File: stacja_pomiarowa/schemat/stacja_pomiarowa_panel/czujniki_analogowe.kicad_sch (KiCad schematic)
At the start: 32 parts, among them J20 Conn_01x03, J21 Conn_01x03, J22 Conn_01x03, J23 Conn_01x03, J24 Conn_01x03, J25 Conn_01x03, J26 Conn_01x03, J27 Conn_01x03, J28 Conn_01x03, J29 Conn_01x03, J30 Conn_01x03, J31 Conn_01x03, J32 Conn_01x03, J33 Conn_01x03, J34 Conn_01x03, J35 Conn_01x03, J36 Conn_01x03, J37 Conn_01x03, J38 Conn_01x03, J39 Conn_01x03, J40 Conn_01x03, J41 Conn_01x03, J42 Conn_01x03, J43 Conn_01x03, J44 Conn_01x03, J45 Conn_01x03, J46 Conn_01x03, J47 Conn_01x03, J48 Conn_01x03, J49 Conn_01x03, J50 Conn_01x03, J51 Conn_01x03

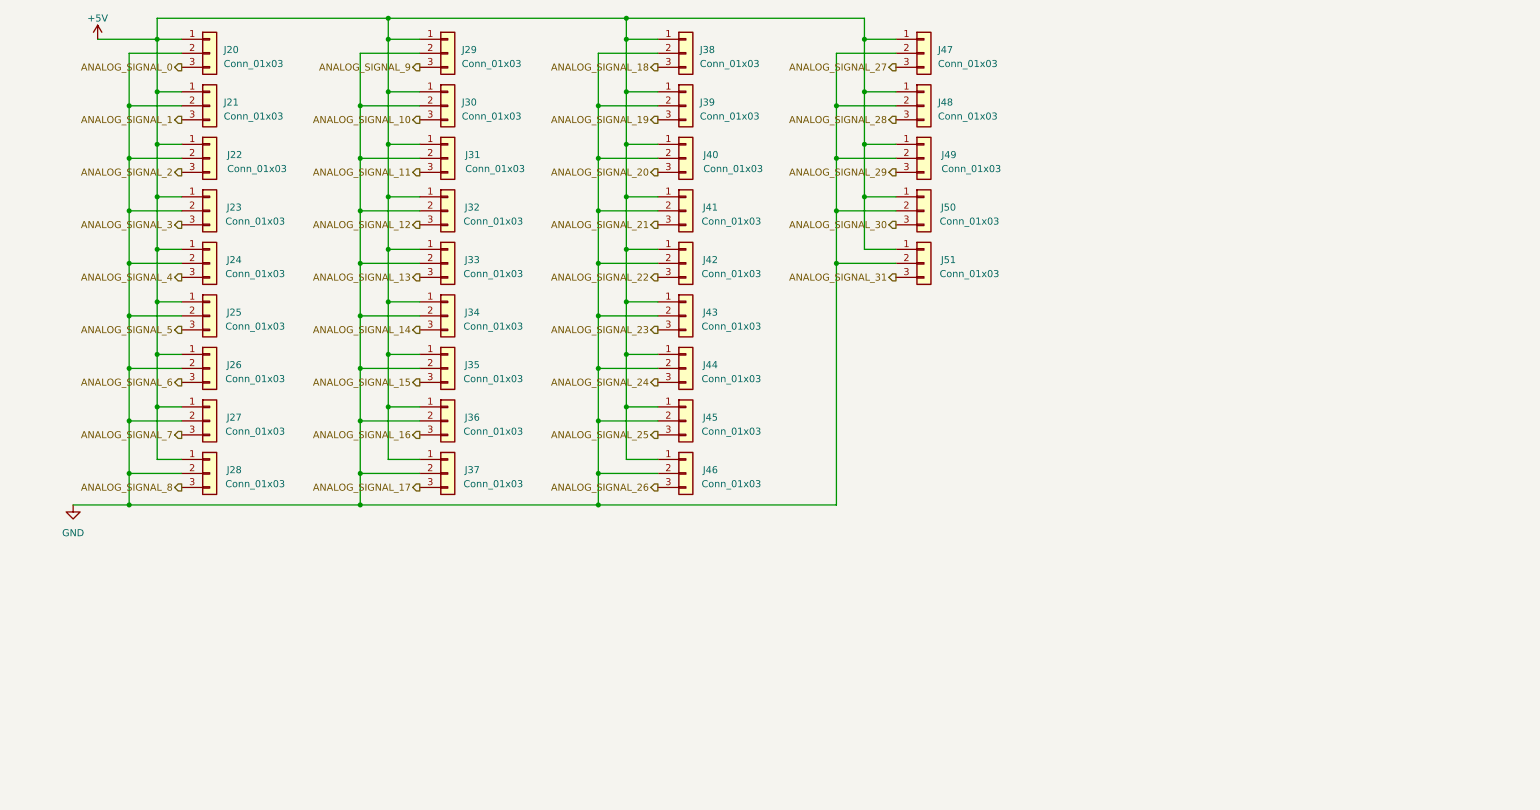
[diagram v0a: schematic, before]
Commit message: Poprawa schematu
Poprzednia numeracja wyjsc analogowych, dodany brakujacy tranzystor Q1, dodane brakujace oporniki podciagajace dla 1-wire i dht11, usuniete oporniki sciagajace dla wyjsc a[0..1] adc - w ten sposob przy niepodlaczonym czujniki nie bedzie stanu niskiego zamiast tego dodane oproniki sciagajace do zlacz dla czujnikow analogowych
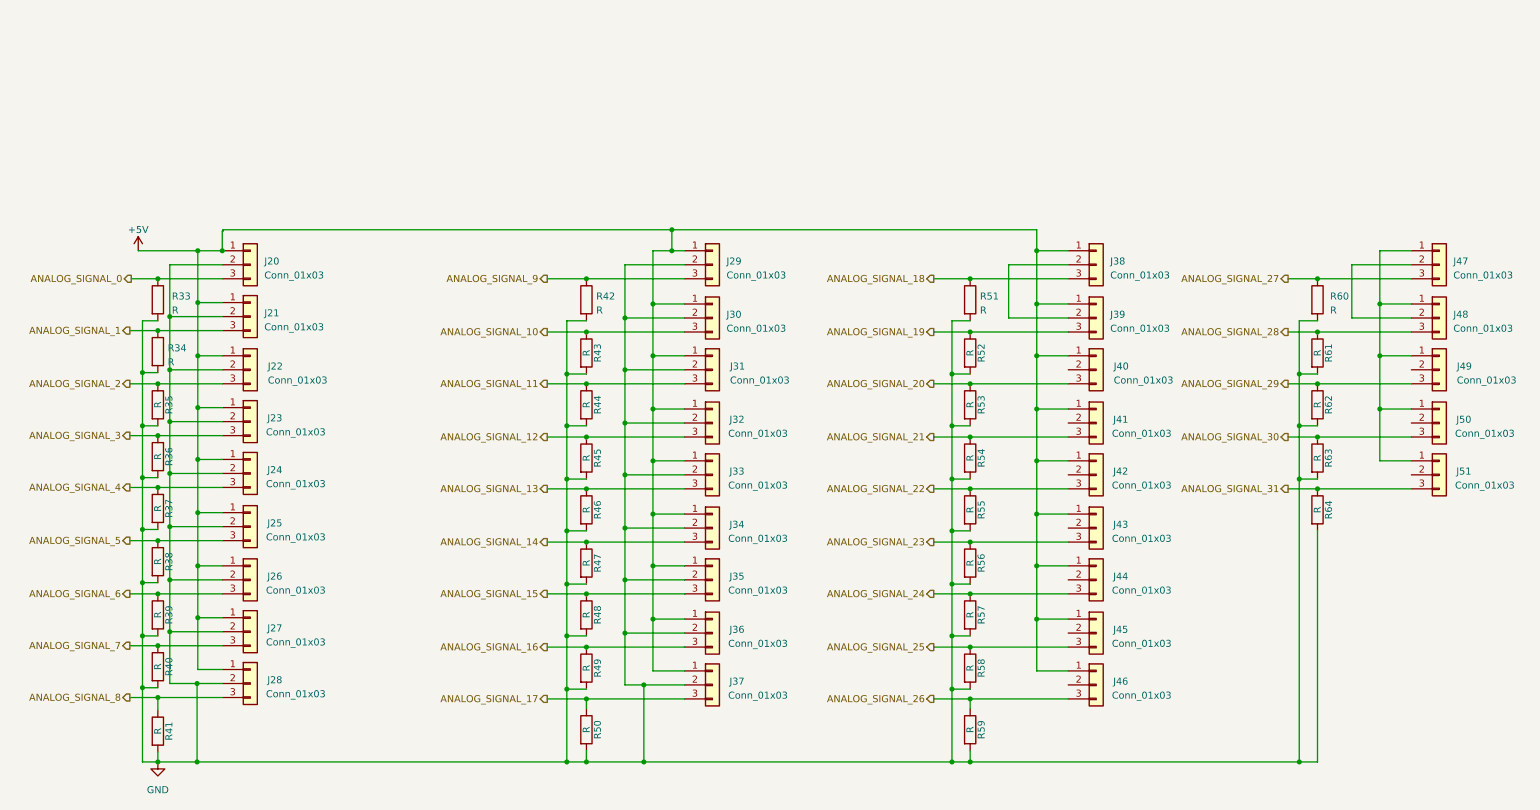
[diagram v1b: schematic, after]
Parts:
- added R33, R34, R35, R36, R37, R38, R39, R40, R41, R42, R43, R44, R45, R46, R47, R48, R49, R50, R51, R52, R53, R54, R55, R56, R57, R58, R59, R60, R61, R62, R63, R64: R, symbol Device:R
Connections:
- net +5V: no longer J47.1 (Pin_1), J48.1 (Pin_1), J49.1 (Pin_1), J50.1 (Pin_1), J51.1 (Pin_1)
- net ANALOG_SIGNAL_0: now also R33.1
- net ANALOG_SIGNAL_1: now also R34.1
- net ANALOG_SIGNAL_10: now also R43.1
- net ANALOG_SIGNAL_11: now also R44.1
- net ANALOG_SIGNAL_12: now also R45.1
- net ANALOG_SIGNAL_13: now also R46.1
- net ANALOG_SIGNAL_14: now also R47.1
- net ANALOG_SIGNAL_15: now also R48.1
- net ANALOG_SIGNAL_16: now also R49.1
- net ANALOG_SIGNAL_17: now also R50.1
- net ANALOG_SIGNAL_18: now also R51.1
- net ANALOG_SIGNAL_19: now also R52.1
- net ANALOG_SIGNAL_2: now also R35.1
- net ANALOG_SIGNAL_20: now also R53.1
- net ANALOG_SIGNAL_21: now also R54.1
- net ANALOG_SIGNAL_22: now also R55.1
- net ANALOG_SIGNAL_23: now also R56.1
- net ANALOG_SIGNAL_24: now also R57.1
- net ANALOG_SIGNAL_25: now also R58.1
- net ANALOG_SIGNAL_26: now also R59.1
- net ANALOG_SIGNAL_27: now also R60.1
- net ANALOG_SIGNAL_28: now also R61.1
- net ANALOG_SIGNAL_29: now also R62.1
- net ANALOG_SIGNAL_3: now also R36.1
- net ANALOG_SIGNAL_30: now also R63.1
- net ANALOG_SIGNAL_31: now also R64.1
- net ANALOG_SIGNAL_4: now also R37.1
- net ANALOG_SIGNAL_5: now also R38.1
- net ANALOG_SIGNAL_6: now also R39.1
- net ANALOG_SIGNAL_7: now also R40.1
- net ANALOG_SIGNAL_8: now also R41.1
- net ANALOG_SIGNAL_9: now also R42.1
- net GND: now also R33.2, R34.2, R35.2, R36.2, R37.2, R38.2, R39.2, R40.2, R41.2, R42.2, R43.2, R44.2, R45.2, R46.2, R47.2, R48.2, R49.2, R50.2, R51.2, R52.2, R53.2, R54.2, R55.2, R56.2, R57.2, R58.2, R59.2, R60.2, R61.2, R62.2, R63.2, R64.2; no longer J38.2 (Pin_2), J39.2 (Pin_2), J40.2 (Pin_2), J41.2 (Pin_2), J42.2 (Pin_2), J43.2 (Pin_2), J44.2 (Pin_2), J45.2 (Pin_2), J46.2 (Pin_2), J47.2 (Pin_2), J48.2 (Pin_2), J49.2 (Pin_2), J50.2 (Pin_2), J51.2 (Pin_2)
- new net: J47.1 (Pin_1), J48.1 (Pin_1), J49.1 (Pin_1), J50.1 (Pin_1), J51.1 (Pin_1)
- new net: J47.2 (Pin_2), J48.2 (Pin_2)
- new net: J38.2 (Pin_2), J39.2 (Pin_2)
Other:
- moved on the sheet: J20, J21, J22, J23, J24, J25, J26, J27, J28, J29, J30, J31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

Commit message: Przywrócono oporniki do wejść ads1115, dodano brakujące oporniki do wejść multipleksera od dht11
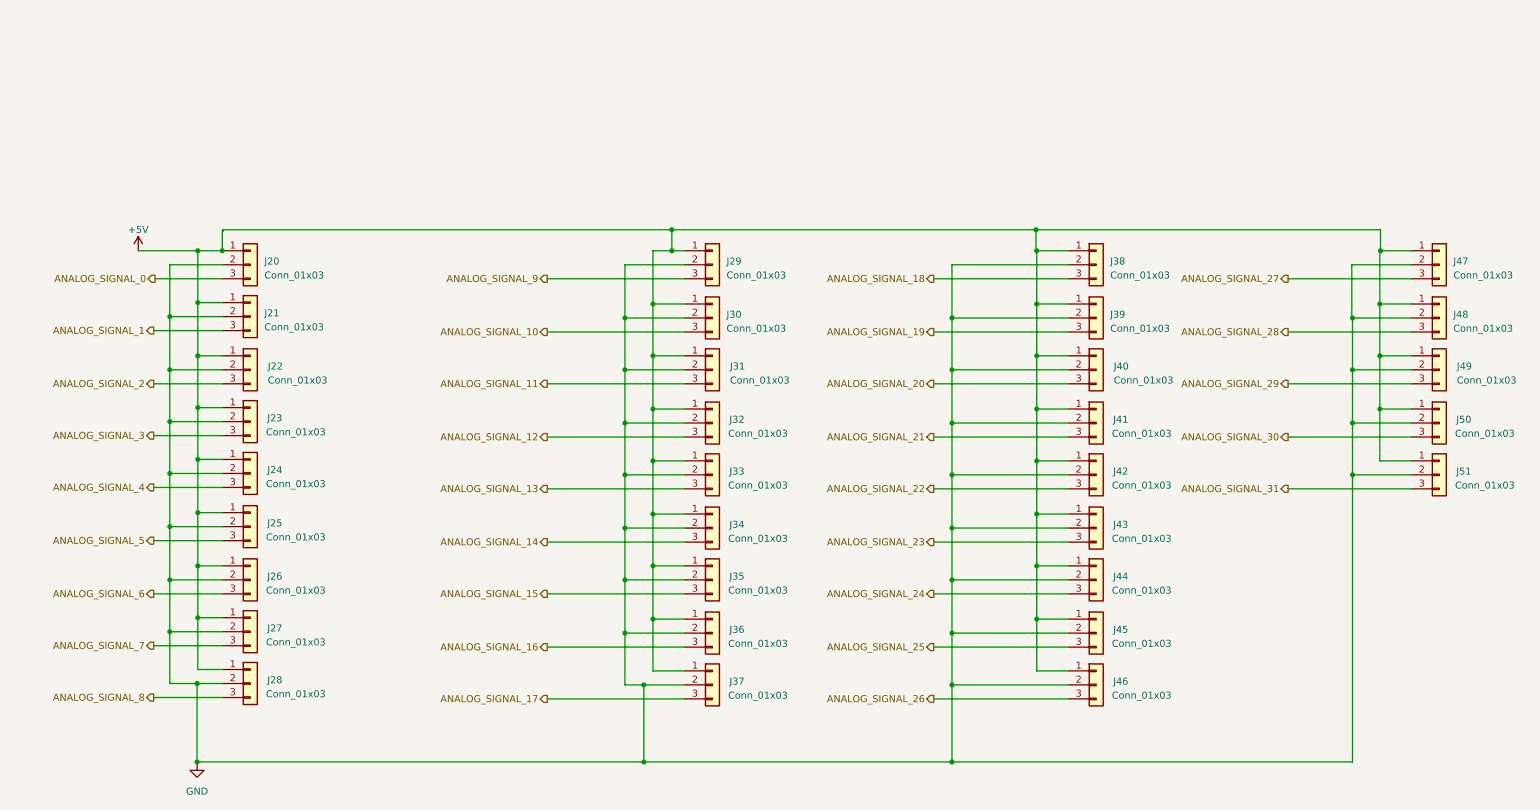
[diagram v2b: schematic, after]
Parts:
- removed R33, R34, R35, R36, R37, R38, R39, R40, R41, R42, R43, R44, R45, R46, R47, R48, R49, R50, R51, R52, R53, R54, R55, R56, R57, R58, R59, R60, R61, R62, R63, R64: R, symbol Device:R
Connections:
- net +5V: now also J47.1 (Pin_1), J48.1 (Pin_1), J49.1 (Pin_1), J50.1 (Pin_1), J51.1 (Pin_1)
- net GND: now also J38.2 (Pin_2), J39.2 (Pin_2), J40.2 (Pin_2), J41.2 (Pin_2), J42.2 (Pin_2), J43.2 (Pin_2), J44.2 (Pin_2), J45.2 (Pin_2), J46.2 (Pin_2), J47.2 (Pin_2), J48.2 (Pin_2), J49.2 (Pin_2), J50.2 (Pin_2), J51.2 (Pin_2)

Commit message: Dodano ledy informujące czy urządzenie połączyło się z systemem, dodane tytuły podschematów ze złączami
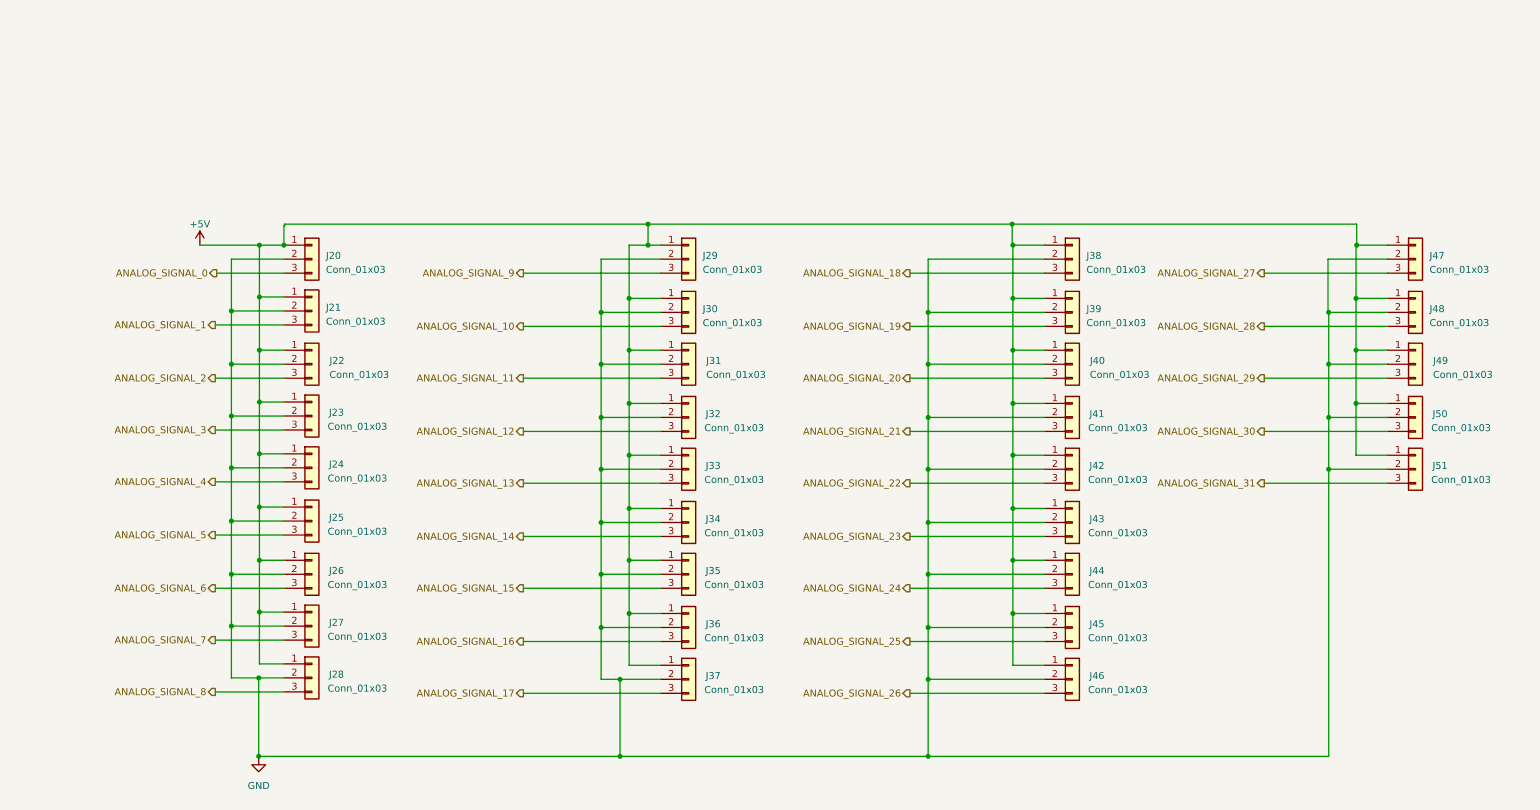
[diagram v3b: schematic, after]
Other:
- title: (none) -> Złącza dla czujników analogowych
- moved on the sheet: J20, J21, J22, J23, J24, J25, J26, J27, J28, J29, J30, J31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
